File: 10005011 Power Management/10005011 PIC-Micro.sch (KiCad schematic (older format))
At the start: 41 parts, among them IC1 LM393D, IC3 PIC18F6622, IC5 DS2480B, J2 ICSP, T2 IRLML5103

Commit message: IC1 conflict
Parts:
- IC1: value LM393 -> LM393D
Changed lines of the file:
@@
 P 8900 3300
 F 0 "IC1" H 8900 2933 50  0000 C CNN
-F 1 "LM393" H 8900 3024 50  0000 C CNN
+F 1 "LM393D" H 8900 3024 50  0000 C CNN
 F 2 "10005011 Power Management:MX.A8_COMPOSANT_1" H 8900 3300 50  0001 C CNN
 F 3 "http://www.ti.com/lit/ds/symlink/lm393-n.pdf" H 8900 3300 50  0001 C CNN

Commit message: IC1 conflict again
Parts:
- IC1: value LM393 -> LM393D
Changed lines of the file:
@@
 P 9500 2300
 F 0 "IC1" H 9458 2346 50  0000 L CNN
-F 1 "LM393" H 9458 2255 50  0000 L CNN
+F 1 "LM393D" H 9458 2255 50  0000 L CNN
 F 2 "10005011 Power Management:MX.A8_COMPOSANT_1" H 9500 2300 50  0001 C CNN
 F 3 "http://www.ti.com/lit/ds/symlink/lm393-n.pdf" H 9500 2300 50  0001 C CNN

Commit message: Powermanagement dev sheet1
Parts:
- D1: footprint 10005011 Power Management:SOT23-1G_1 -> Package_TO_SOT_SMD:SOT-23; symbol Device:D_Schottky -> 10005011_Power_Management:BAT54; Description (none) -> DIODE SCHOTTKY 30V 200MA SOT23-3; Item Number (none) -> 10022652; Mfgr (none) -> ON Semiconductor; Mfgr_PN (none) -> BAT54LT1G; Source (none) -> Digi-Key; Source_PN (none) -> BAT54LT1GOSTR-ND
- T2: symbol Device:Q_PMOS_GSD -> 10005011_Power_Management:IRLML5103TRPBF; Description (none) -> MOSFET P-CH 30V 760MA SOT-23; Item Number (none) -> 10022933; Mfgr (none) -> Infineon Technologies; Mfgr_PN (none) -> IRLML5103TRPBF; Source (none) -> Digi-Key; Source_PN (none) -> IRLML5103PBFCT-ND
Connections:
- net labels removed: PST2, PST3, PST4, PST5, PST6, PST7, PST8
- wire segments 238 -> 199
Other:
- moved on the sheet: C12, C13, C15, C4, C6, C64, IC1A, IC1B, IC1C, PST2, PST3, PST4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

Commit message: Powermanagement dev
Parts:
- C12, C13, C15, C17, C4, C6, C63, C64: Description (none) -> CAPACITOR,100NF,16V,+/-10%,X7R,0402; Item Number (none) -> 10022607; Manufacturer (none) -> MURATA; Manufacturer_No (none) -> GRM155R71C104JA88J
- C16: symbol 10005011_Power_Management_Schematic_Symbols:470pF -> Device:C
- C82: value 0.1uF -> 100nF; symbol 10005011_Power_Management_Schematic_Symbols:0.1uF -> Device:C; Bom_Footprint 0402 -> (none); Description CAP CER 47PF 50V C0G/NP0 0402 -> CAPACITOR,100NF,16V,+/-10%,X7R,0402; Item Number (none) -> 10022607; Manufacturer (none) -> MURATA; Manufacturer_No (none) -> GRM155R71C104JA88J
- CT1: value ERT-J1VR103J -> B57164K103J; symbol 10005011_Power_Management_Schematic_Symbols:Thermistor_NTC_10k_4250K -> Device:Thermistor_NTC; Bom_Footprint 0603 -> (none); Description THERMISTOR NTC 10KOHM 4250K 0603 -> THERMISTOR, 10K OHM, B4300. +/-5%; Item Number (none) -> 10022929; Mfgr_PN ERT-J1VR103J -> B57164K103J; Source_PN P10547CT-ND -> 495-2080-ND
- D1: footprint Package_TO_SOT_SMD:SOT-23 -> 10005011 Power Management:SOT23-1G_1
- IC3: symbol page1:PIC18F6622 -> 10005011_Power_Management:PIC18F6622; Description (none) -> MICROCON,8 BIT, FLASH 64K,RAM3966 BYTES,TQFP64; Item Number (none) -> 10022888; Manufacturer (none) -> MICROCHIP TECHNOLOGY; Manufacturer_No (none) -> PIC18F6622-I/PT
- IC5: symbol page1:DS2480B -> 10005011_Power_Management:DS2480B; Description (none) -> IC, SERIAL TO 1-WIRE DRIVER, SOIC8; Item Number (none) -> 10022890; Manufacturer (none) -> MAXIM; Manufacturer_No (none) -> DS2480B+T&R
- ML5: symbol 10005011_Power_Management_Schematic_Symbols:B72500T0040M060 -> Device:Varistor; Bom_Footprint 0603 -> (none)
- R11: symbol 10005011_Power_Management_Schematic_Symbols:100 -> Device:R
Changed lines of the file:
@@
 F 2 "10005011 Power Management:C0402_1" H 2288 1450 50  0001 C CNN
 F 3 "~" H 2250 1600 50  0001 C CNN
+F 4 "CAPACITOR,100NF,16V,+/-10%,X7R,0402" H 2250 1600 50  0001 C CNN "Description"
+F 5 "10022607" H 2250 1600 50  0001 C CNN "Item Number"
+F 6 "MURATA" H 2250 1600 50  0001 C CNN "Manufacturer"
+F 7 "GRM155R71C104JA88J" H 2250 1600 50  0001 C CNN "Manufacturer_No"
 	1    2250 1600
 	-1   0    0    1
@@
 F 2 "10005011 Power Management:C0402_1" H 2788 1450 50  0001 C CNN
 F 3 "~" H 2750 1600 50  0001 C CNN
+F 4 "CAPACITOR,100NF,16V,+/-10%,X7R,0402" H 2750 1600 50  0001 C CNN "Description"
+F 5 "10022607" H 2750 1600 50  0001 C CNN "Item Number"
+F 6 "MURATA" H 2750 1600 50  0001 C CNN "Manufacturer"
+F 7 "GRM155R71C104JA88J" H 2750 1600 50  0001 C CNN "Manufacturer_No"
 	1    2750 1600
 	1    0    0    1
@@
 F 2 "10005011 Power Management:C0402_1" H 3288 1450 50  0001 C CNN
 F 3 "~" H 3250 1600 50  0001 C CNN
+F 4 "CAPACITOR,100NF,16V,+/-10%,X7R,0402" H 3250 1600 50  0001 C CNN "Description"
+F 5 "10022607" H 3250 1600 50  0001 C CNN "Item Number"
+F 6 "MURATA" H 3250 1600 50  0001 C CNN "Manufacturer"
+F 7 "GRM155R71C104JA88J" H 3250 1600 50  0001 C CNN "Manufacturer_No"
 	1    3250 1600
 	1    0    0    1
@@
 F 2 "10005011 Power Management:C0402_1" H 3788 1450 50  0001 C CNN
 F 3 "~" H 3750 1600 50  0001 C CNN
+F 4 "CAPACITOR,100NF,16V,+/-10%,X7R,0402" H 3750 1600 50  0001 C CNN "Description"
+F 5 "10022607" H 3750 1600 50  0001 C CNN "Item Number"
+F 6 "MURATA" H 3750 1600 50  0001 C CNN "Manufacturer"
+F 7 "GRM155R71C104JA88J" H 3750 1600 50  0001 C CNN "Manufacturer_No"
 	1    3750 1600
 	1    0    0    -1
@@
 F 2 "10005011 Power Management:C0402_1" H 3188 6350 50  0001 C CNN
 F 3 "~" H 3150 6500 50  0001 C CNN
+F 4 "CAPACITOR,100NF,16V,+/-10%,X7R,0402" H 3150 6500 50  0001 C CNN "Description"
+F 5 "10022607" H 3150 6500 50  0001 C CNN "Item Number"
+F 6 "MURATA" H 3150 6500 50  0001 C CNN "Manufacturer"
+F 7 "GRM155R71C104JA88J" H 3150 6500 50  0001 C CNN "Manufacturer_No"
 	1    3150 6500
 	1    0    0    -1
@@
 Wire Wire Line
 	1800 6850 1800 6750
-Wire Wire Line
-	1800 6850 1800 6950
 Connection ~ 1800 6850
 $Comp
@@
 F 2 "10005011 Power Management:C0402_1" H 2738 6950 50  0001 C CNN
 F 3 "~" H 2700 7100 50  0001 C CNN
+F 4 "CAPACITOR,100NF,16V,+/-10%,X7R,0402" H 2700 7100 50  0001 C CNN "Description"
+F 5 "10022607" H 2700 7100 50  0001 C CNN "Item Number"
+F 6 "MURATA" H 2700 7100 50  0001 C CNN "Manufacturer"
+F 7 "GRM155R71C104JA88J" H 2700 7100 50  0001 C CNN "Manufacturer_No"
 	1    2700 7100
 	1    0    0    -1
@@
 	1    0    0    -1
 $EndComp
-Wire Wire Line
-	1800 7450 1800 7350
 Text Label 1850 6850 0    50   ~ 0
 AMB-TEMP
@@
 F 2 "10005011 Power Management:C0402_1" H 8438 1650 50  0001 C CNN
 F 3 "~" H 8400 1800 50  0001 C CNN
+F 4 "CAPACITOR,100NF,16V,+/-10%,X7R,0402" H 8400 1800 50  0001 C CNN "Description"
+F 5 "10022607" H 8400 1800 50  0001 C CNN "Item Number"
+F 6 "MURATA" H 8400 1800 50  0001 C CNN "Manufacturer"
+F 7 "GRM155R71C104JA88J" H 8400 1800 50  0001 C CNN "Manufacturer_No"
 	1    8400 1800
 	1    0    0    1
@@
 F 2 "10005011 Power Management:C0402_1" H 2088 10200 50  0001 C CNN
 F 3 "~" H 2050 10350 50  0001 C CNN
+F 4 "CAPACITOR,100NF,16V,+/-10%,X7R,0402" H 2050 10350 50  0001 C CNN "Description"
+F 5 "10022607" H 2050 10350 50  0001 C CNN "Item Number"
+F 6 "MURATA" H 2050 10350 50  0001 C CNN "Manufacturer"
+F 7 "GRM155R71C104JA88J" H 2050 10350 50  0001 C CNN "Manufacturer_No"
 	1    2050 10350
 	1    0    0    -1
@@
 U 1 1 5FEC9584
 P 4050 9400
-F 0 "D1" H 4000 9085 50  0000 C CNN
-F 1 "BAT54" H 4000 9176 50  0000 C CNN
-F 2 "Package_TO_SOT_SMD:SOT-23" H 3820 9238 50  0001 L CNN
+F 0 "D1" H 4000 9219 50  0000 C CNN
+F 1 "BAT54" H 4000 9310 50  0000 C CNN
+F 2 "10005011 Power Management:SOT23-1G_1" H 3820 9238 50  0001 L CNN
 F 3 "http://www.onsemi.com/pub/Collateral/BAT54LT1-D.PDF" H 3970 9500 50  0001 C CNN
 F 4 "DIODE SCHOTTKY 30V 200MA SOT23-3" H 4375 9225 60  0001 C CNN "Description"
@@
 Wire Wire Line
 	4000 10400 4400 10400
-Text Notes 1600 7150 1    50   ~ 0
+Text Notes 1600 7450 1    50   ~ 0
 Ambient temperature\nmeasurement
 Text Notes 2500 1100 0    50   ~ 0
@@
 	1950 9500 3400 9500
 $Comp
-L 10005011_Power_Management_Schematic_Symbols:Thermistor_NTC_10k_4250K CT1
+L Device:Thermistor_NTC CT1
 U 1 1 5E9166E0
 P 1800 7150
 F 0 "CT1" H 1905 7150 50  0000 L CNN
-F 1 "ERT-J1VR103J" H 1905 7105 50  0001 L CNN
+F 1 "B57164K103J" H 1905 7105 50  0001 L CNN
 F 2 "10005011 Power Management:K164_1" H 1800 7150 50  0001 C CNN
-F 3 "http://industrial.panasonic.com/www-cgi/jvcr13pz.cgi?E+PZ+3+AUA0001+ERTJ1VR103J+7+WW" H 1800 7150 50  0001 C CNN
+F 3 "https://www.tdk-electronics.tdk.com/inf/50/db/ntc/NTC_Leaded_disks_K164.pdf" H 1800 7150 50  0001 C CNN
 F 4 "Panasonic Electronic Components" H 1800 7150 50  0001 C CNN "Mfgr"
-F 5 "ERT-J1VR103J" H 1800 7150 50  0001 C CNN "Mfgr_PN"
+F 5 "B57164K103J" H 1800 7150 50  0001 C CNN "Mfgr_PN"
 F 6 "Digi-Key" H 1800 7150 50  0001 C CNN "Source"
-F 7 "P10547CT-ND" H 1800 7150 50  0001 C CNN "Source_PN"
-F 8 "THERMISTOR NTC 10KOHM 4250K 0603" H 1800 7150 50  0001 C CNN "Description"
-F 9 "0603" H 1800 7150 50  0001 C CNN "Bom_Footprint"
+F 7 "495-2080-ND" H 1800 7150 50  0001 C CNN "Source_PN"
+F 8 "THERMISTOR, 10K OHM, B4300. +/-5%" H 1800 7150 50  0001 C CNN "Description"
+F 9 "10022929" H 1800 7150 50  0001 C CNN "Item Number"
 	1    1800 7150
 	1    0    0    1
@@
 	3400 10400 4000 10400
 $Comp
-L page1:DS2480B IC5
+L 10005011_Power_Management:DS2480B IC5
 U 1 1 60260D1A
 P 13700 6950
@@
 F 2 "10005011 Power Management:MX.A8_COMPOSANT_1" H 13550 7700 50  0001 C CNN
 F 3 "https://datasheets.maximintegrated.com/en/ds/DS2480B.pdf" H 13600 7150 50  0001 C CNN
+F 4 "IC, SERIAL TO 1-WIRE DRIVER, SOIC8" H 13700 6950 50  0001 C CNN "Description"
+F 5 "10022890" H 13700 6950 50  0001 C CNN "Item Number"
+F 6 "MAXIM" H 13700 6950 50  0001 C CNN "Manufacturer"
+F 7 "DS2480B+T&R" H 13700 6950 50  0001 C CNN "Manufacturer_No"
 	1    13700 6950
 	1    0    0    -1
 $EndComp
 $Comp
-L 10005011_Power_Management_Schematic_Symbols:100 R11
+L Device:R R11
 U 1 1 60260D1B
 P 12450 7050
@@
 	12600 7050 12800 7050
 $Comp
-L 10005011_Power_Management_Schematic_Symbols:470pF C16
+L Device:C C16
 U 1 1 60260D1C
 P 12100 7300
@@
 	12100 7450 12100 7650
 $Comp
-L 10005011_Power_Management_Schematic_Symbols:0.1uF C82
+L Device:C C82
 U 1 1 60260D1E
 P 13000 6500
 F 0 "C82" H 12886 6546 50  0000 R CNN
-F 1 "0.1uF" H 12886 6455 50  0000 R CNN
+F 1 "100nF" H 12886 6455 50  0000 R CNN
 F 2 "10005011 Power Management:C0402_1" H 13038 6350 50  0001 C CNN
 F 3 "https://psearch.en.murata.com/capacitor/product/GCM155R71C104KA55%23.pdf" H 13000 6500 50  0001 C CNN
@@
 F 6 "Digi-Key" H 13000 6500 50  0001 C CNN "Source"
 F 7 "490-7998-1-ND" H 13000 6500 50  0001 C CNN "Source_PN"
-F 8 "0402" H 12886 6455 50  0001 R CNN "Bom_Footprint"
-F 9 "CAP CER 47PF 50V C0G/NP0 0402" H 13000 6500 50  0001 C CNN "Description"
+F 8 "" H 12886 6455 50  0001 R CNN "Bom_Footprint"
+F 9 "CAPACITOR,100NF,16V,+/-10%,X7R,0402" H 13000 6500 50  0001 C CNN "Description"
 F 10 "X7R" H 13000 6500 50  0001 C CNN "Dielectric"
 F 11 "16V" H 12886 6364 50  0001 R CNN "Voltage"
+F 12 "10022607" H 13000 6500 50  0001 C CNN "Item Number"
+F 13 "MURATA" H 13000 6500 50  0001 C CNN "Manufacturer"
+F 14 "GRM155R71C104JA88J" H 13000 6500 50  0001 C CNN "Manufacturer_No"
 	1    13000 6500
 	1    0    0    -1
@@
 	14200 6650 15100 6650
 $Comp
-L 10005011_Power_Management_Schematic_Symbols:B72500T0040M060 ML5
+L Device:Varistor ML5
 U 1 1 5E931E5C
 P 12800 7400
@@
 F 7 "B72500T0040M060" H 12800 7400 50  0001 C CNN "Mfgr_PN"
 F 8 "VARISTOR 8V 30A 0603" H 12800 7400 50  0001 C CNN "Description"
-F 9 "0603" H 12903 7309 50  0001 L CNN "Bom_Footprint"
 	1    12800 7400
 	1    0    0    1
@@
 Connection ~ 4400 9500
 $Comp
-L page1:PIC18F6622 IC3
+L 10005011_Power_Management:PIC18F6622 IC3
 U 1 1 5FEC9553
 P 4150 4600
@@
 F 2 "10005011 Power Management:TQFP64_1" H 4150 3050 50  0001 C CIN
 F 3 "http://ww1.microchip.com/downloads/en/DeviceDoc/39646c.pdf" H 650 4200 50  0001 C CNN
+F 4 "MICROCON,8 BIT, FLASH 64K,RAM3966 BYTES,TQFP64" H 4150 4600 50  0001 C CNN "Description"
+F 5 "10022888" H 4150 4600 50  0001 C CNN "Item Number"
+F 6 "MICROCHIP TECHNOLOGY" H 4150 4600 50  0001 C CNN "Manufacturer"
+F 7 "PIC18F6622-I/PT" H 4150 4600 50  0001 C CNN "Manufacturer_No"
 	1    4150 4600
 	1    0    0    -1
 $EndComp
+Wire Wire Line
+	1800 6850 1800 7000
+Wire Wire Line
+	1800 7300 1800 7450
 $EndSCHEMATC

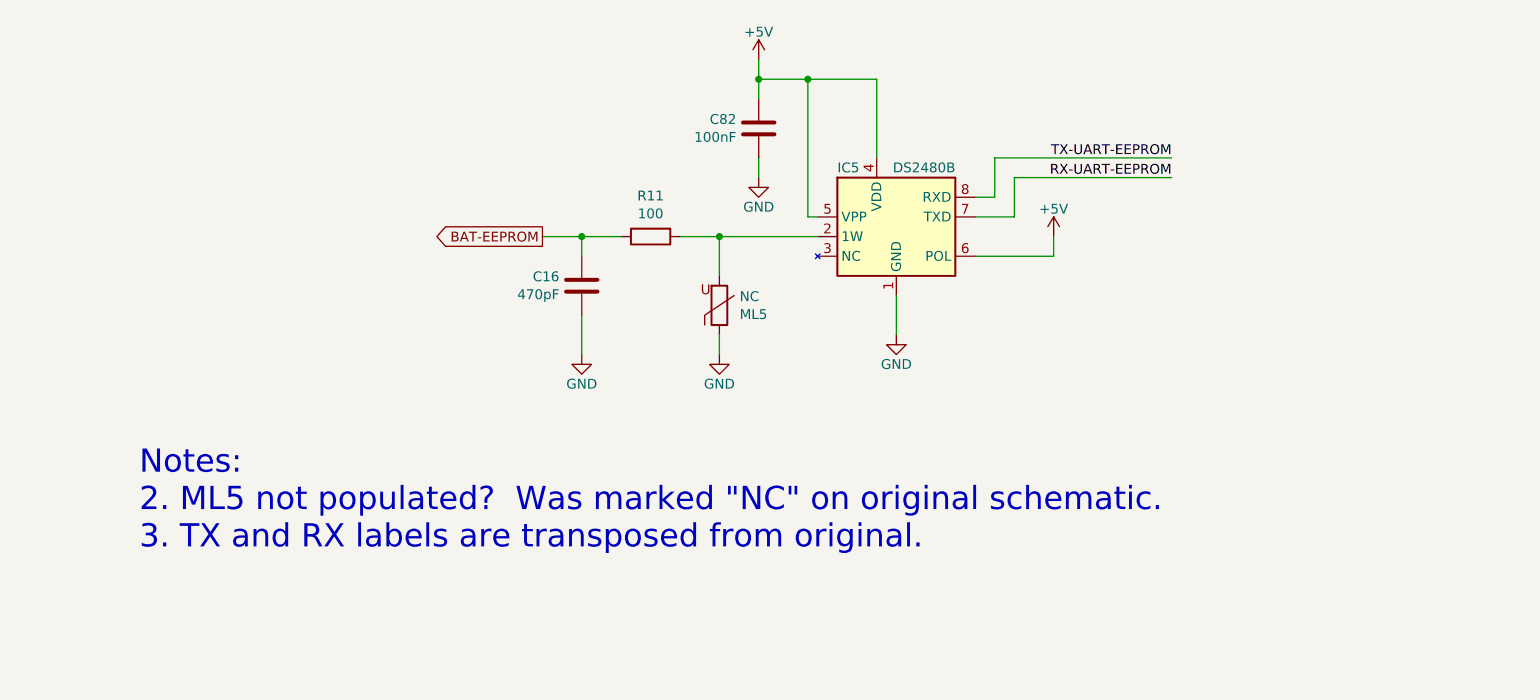
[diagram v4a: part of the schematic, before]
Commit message: update PCB deleting double lines in the edge layer to create a board outline and update the USB_A footprints and IC11
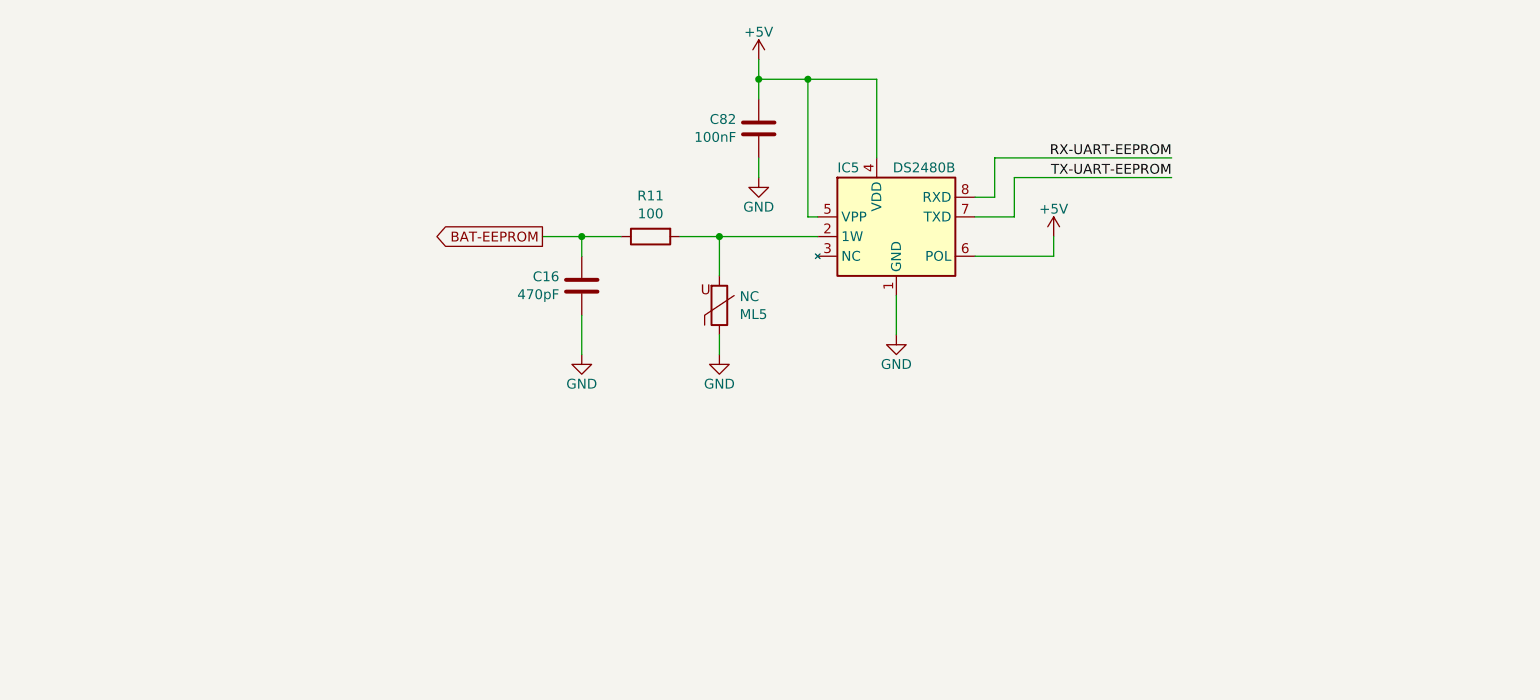
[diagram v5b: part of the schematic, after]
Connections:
- net RX-UART-EEPROM: now also IC5.8 (RXD); no longer IC5.7 (TXD)
- net TX-UART-EEPROM: now also IC5.7 (TXD); no longer IC5.8 (RXD)
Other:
- note removed: "Notes:\n2. ML5 not populated? Was marked "NC" on original schematic.\n3. TX and RX labels are transposed from original."
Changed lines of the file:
@@
 	1    0    0    1
 $EndComp
-Text Notes 9850 8650 0    118  ~ 0
-Notes:\n2. ML5 not populated?  Was marked "NC" on original schematic.\n3. TX and RX labels are transposed from original.
 $Comp
 L power:GND #PWR0279
@@
 Wire Wire Line
 	5050 4650 5500 4650
+Text Label 15100 6750 2    50   ~ 0
+TX-UART-EEPROM
 Text Label 15100 6650 2    50   ~ 0
-TX-UART-EEPROM
-Text Label 15100 6750 2    50   ~ 0
 RX-UART-EEPROM
 Text GLabel 11900 7050 0    50   Output ~ 0

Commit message: change CR1-BIS to ZCR1 so that kicad does not think it is missing annotation, do the same in the PCB to be able to read netlist without components getting erased and placed new
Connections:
- net 5VPIC renamed +5VPIC
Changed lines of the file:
@@
 Wire Wire Line
 	4250 2650 4250 2450
-Connection ~ 3950 2450
 Wire Wire Line
 	3950 2450 3950 2650
@@
 Wire Wire Line
 	5150 3450 5050 3450
-Wire Wire Line
-	3550 2450 3950 2450
 $Comp
 L Connector:TestPoint_Alt PST8
@@
 	-1   0    0    1
 $EndComp
-Wire Wire Line
-	9800 3400 9900 3400
 $Comp
 L Comparator:LM393 IC1
@@
 Text Notes 1600 7450 1    50   ~ 0
 Ambient temperature\nmeasurement
-Text Notes 2500 1100 0    50   ~ 0
+Text Notes 1900 1150 0    50   ~ 0
 PIC bypass capacitors
 Text Label 9100 4850 0    50   ~ 0
@@
 ICSP-PWR
 Wire Wire Line
-	2750 1250 3250 1250
-Text Label 2400 1250 0    50   ~ 0
-5VPIC
-Wire Wire Line
 	1950 9200 2300 9200
 Text Label 2300 9200 2    50   ~ 0
@@
 Wire Wire Line
 	1950 9300 2300 9300
-Text Label 3550 2450 0    50   ~ 0
-5VPIC
-Text Label 4700 9500 2    50   ~ 0
-5VPIC
 Text Label 2300 9600 2    50   ~ 0
 MCLR
@@
 Text GLabel 2500 5550 0    50   Input ~ 0
 MES-VACDC
-Text GLabel 1700 5750 0    50   Input ~ 0
-+3.0VREF
 Text GLabel 2500 5850 0    50   Input ~ 0
 MES-3.3V
@@
 Text GLabel 9900 3200 2    50   Input ~ 0
 MES-VDC
-Text GLabel 9900 3400 2    50   Input ~ 0
-+3.0VREF
 Text GLabel 9900 4650 2    50   Input ~ 0
 MES-VACDC
-Text GLabel 9900 4850 2    50   Input ~ 0
-+3.0VREF
 Text GLabel 5350 4150 2    50   Output ~ 0
 LED-AC-PRESENCE
@@
 Wire Wire Line
 	1800 7300 1800 7450
+$Comp
+L 10005011_Power_Management:+3.0VREF #PWR0289
+U 1 1 5E987469
+P 1700 5700
+F 0 "#PWR0289" H 1700 5550 50  0001 C CNN
+F 1 "+3.0VREF" H 1715 5873 50  0000 C CNN
+F 2 "" H 1700 5700 50  0001 C CNN
+F 3 "" H 1700 5700 50  0001 C CNN
+	1    1700 5700
+	1    0    0    -1
+$EndComp
+Wire Wire Line
+	1700 5700 1700 5750
+$Comp
+L 10005011_Power_Management:+3.0VREF #PWR0290
+U 1 1 5EA52332
+P 10150 3500
+F 0 "#PWR0290" H 10150 3350 50  0001 C CNN
+F 1 "+3.0VREF" H 10165 3673 50  0000 C CNN
+F 2 "" H 10150 3500 50  0001 C CNN
+F 3 "" H 10150 3500 50  0001 C CNN
+	1    10150 3500
+	1    0    0    -1
+$EndComp
+Wire Wire Line
+	10150 3500 10150 3550
+Wire Wire Line
+	10150 3550 9950 3550
+Wire Wire Line
+	9950 3550 9950 3400
+Wire Wire Line
+	9800 3400 9950 3400
+$Comp
+L 10005011_Power_Management:+3.0VREF #PWR0291
+U 1 1 5EA5F26B
+P 10100 4950
+F 0 "#PWR0291" H 10100 4800 50  0001 C CNN
+F 1 "+3.0VREF" H 10115 5123 50  0000 C CNN
+F 2 "" H 10100 4950 50  0001 C CNN
+F 3 "" H 10100 4950 50  0001 C CNN
+	1    10100 4950
+	1    0    0    -1
+$EndComp
+Wire Wire Line
+	10100 4950 10100 5000
+Wire Wire Line
+	10100 5000 9900 5000
+Wire Wire Line
+	9900 5000 9900 4850
+$Comp
+L 10005011_Power_Management:+5VPIC #PWR0292
+U 1 1 5EA7F0FF
+P 4150 2350
+F 0 "#PWR0292" H 4150 2200 50  0001 C CNN
+F 1 "+5VPIC" H 4165 2523 50  0000 C CNN
+F 2 "" H 4150 2350 50  0001 C CNN
+F 3 "" H 4150 2350 50  0001 C CNN
+	1    4150 2350
+	1    0    0    -1
+$EndComp
+Wire Wire Line
+	4150 2350 4150 2450
+$Comp
+L 10005011_Power_Management:+5VPIC #PWR0293
+U 1 1 5EA97614
+P 3000 1150
+F 0 "#PWR0293" H 3000 1000 50  0001 C CNN
+F 1 "+5VPIC" H 3015 1323 50  0000 C CNN
+F 2 "" H 3000 1150 50  0001 C CNN
+F 3 "" H 3000 1150 50  0001 C CNN
+	1    3000 1150
+	1    0    0    -1
+$EndComp
+Wire Wire Line
+	3000 1150 3000 1250
+Wire Wire Line
+	2750 1250 3000 1250
+Connection ~ 3000 1250
+Wire Wire Line
+	3000 1250 3250 1250
+$Comp
+L 10005011_Power_Management:+5VPIC #PWR0294
+U 1 1 5EAB1137
+P 4700 9450
+F 0 "#PWR0294" H 4700 9300 50  0001 C CNN
+F 1 "+5VPIC" H 4715 9623 50  0000 C CNN
+F 2 "" H 4700 9450 50  0001 C CNN
+F 3 "" H 4700 9450 50  0001 C CNN
+	1    4700 9450
+	1    0    0    -1
+$EndComp
+Wire Wire Line
+	4700 9450 4700 9500
 $EndSCHEMATC

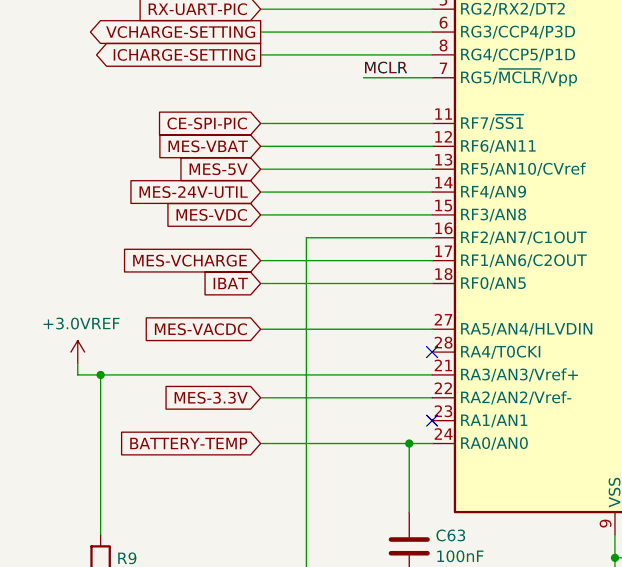
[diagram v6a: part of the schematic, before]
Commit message: (Trying again on a new branch - something broke last time) adding Altium PCB and imported kicad_pcb, plus import log
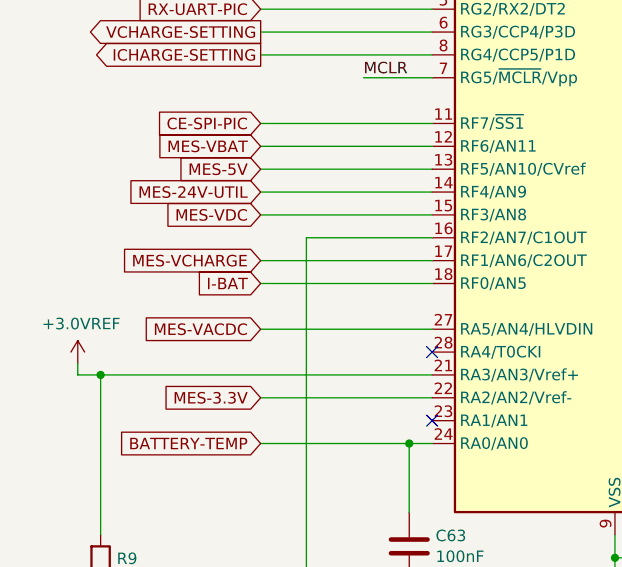
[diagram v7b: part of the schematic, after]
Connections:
- net IBAT renamed I-BAT
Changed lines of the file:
@@
 MES-VCHARGE
 Text GLabel 2500 5350 0    50   Input ~ 0
-IBAT
+I-BAT
 Text GLabel 2500 5550 0    50   Input ~ 0
 MES-VACDC
